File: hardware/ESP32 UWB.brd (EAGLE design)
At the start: 72.3 x 32.6 mm, 55 parts, among them J2 HEADER-12P-2.54, J4 10118194-0001LF, Q3 S8050, Q4 S8050, U1 SILICON_LABS_CP2102N-A01-GQFN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, U2 V_REG_MIC2920, U5 DWM1000, U6 ESP32-C3-MINI-1-N4

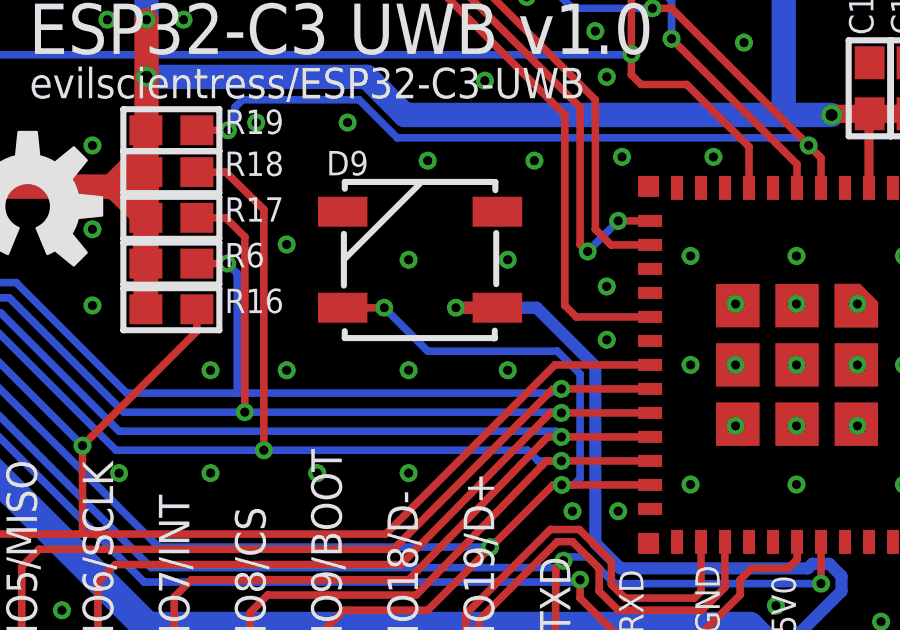
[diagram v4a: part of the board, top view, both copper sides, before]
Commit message: added solder jumper for optionally disabling the ws2812 led
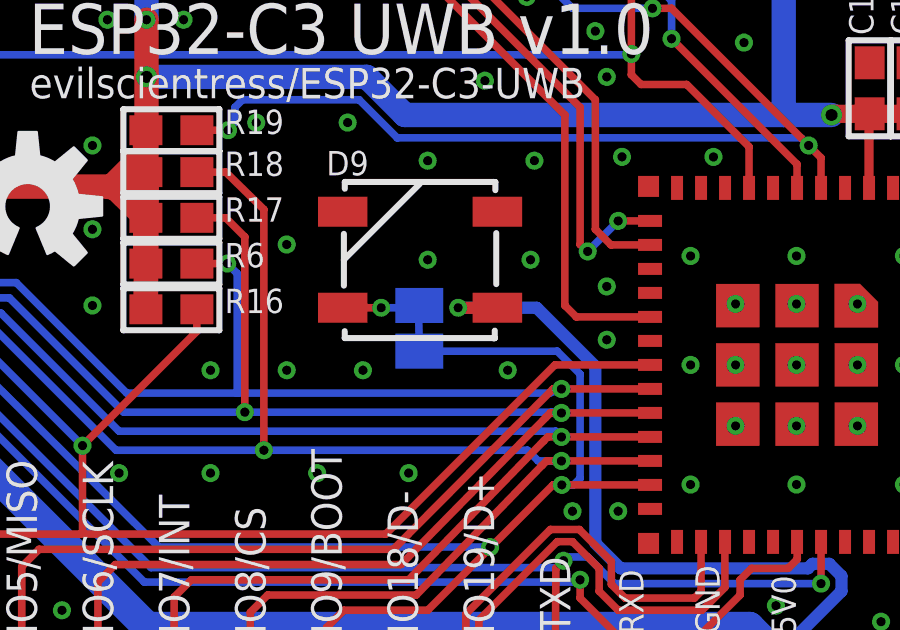
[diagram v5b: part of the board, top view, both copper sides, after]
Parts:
- added SJ1: (no value), jumper:SJ
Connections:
- net IO9: now also SJ1.1, SJ1.2
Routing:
- net IO9: track 96.9 -> 97.8 mm
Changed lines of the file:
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@@
 <setting verticaltext="up"/>
 </settings>
-<grid distance="10" unitdist="mil" unit="mm" style="dots" multiple="1" display="yes" altdistance="1" altunitdist="mil" altunit="mil"/>
+<grid distance="10" unitdist="mil" unit="mil" style="dots" multiple="1" display="yes" altdistance="1" altunitdist="mil" altunit="mil"/>
 <layers>
 <layer number="1" name="Top" color="4" fill="1" visible="yes" active="yes"/>
@@
 <attribute name="VALUE" x="49.594" y="18.11" size="0.6096" layer="27" rot="R180"/>
 </element>
+<element name="SJ1" library="jumper" package="SJ" value="" x="53.8226" y="14.224" smashed="yes" rot="MR90">
+<attribute name="NAME" x="54.9656" y="12.573" size="0.8128" layer="26" font="vector" ratio="18" rot="MR90"/>
+<attribute name="VALUE" x="53.8226" y="14.6241" size="0.02" layer="28" rot="MR90"/>
+</element>
 </elements>
 <signals>
@@
 <via x="56.769" y="12.827" extent="1-16" drill="0.3048"/>
 <via x="53.467" y="9.398" extent="1-16" drill="0.3048"/>
-<via x="53.467" y="12.827" extent="1-16" drill="0.3048"/>
+<via x="51.943" y="12.827" extent="1-16" drill="0.3048"/>
 <via x="43.815" y="9.398" extent="1-16" drill="0.3048"/>
 <via x="42.926" y="17.526" extent="1-16" drill="0.3048"/>
@@
 <contactref element="D9" pad="3"/>
 <via x="58.928" y="8.128" extent="1-16" drill="0.3048"/>
-<via x="56.769" y="16.51" extent="1-16" drill="0.3048"/>
-<via x="53.467" y="16.51" extent="1-16" drill="0.3048"/>
+<via x="57.531" y="16.51" extent="1-16" drill="0.3048"/>
+<via x="54.102" y="16.51" extent="1-16" drill="0.3048"/>
 <contactref element="U1" pad="2"/>
 <contactref element="U1" pad="23"/>
@@
 <contactref element="D6" pad="-"/>
 <contactref element="D9" pad="1"/>
-<wire x1="56.425" y1="14.91" x2="55.042" y2="14.91" width="0.4064" layer="1"/>
-<via x="55.042" y="14.91" extent="1-16" drill="0.3"/>
-<wire x1="55.042" y1="14.91" x2="57.734" y2="14.91" width="0.4064" layer="16"/>
+<wire x1="56.425" y1="14.91" x2="55.1182" y2="14.91" width="0.4064" layer="1"/>
+<via x="55.1182" y="14.91" extent="1-16" drill="0.3"/>
+<wire x1="55.1182" y1="14.91" x2="57.734" y2="14.91" width="0.4064" layer="16"/>
 <wire x1="57.734" y1="14.91" x2="59.69" y2="12.954" width="0.4064" layer="16"/>
 <wire x1="59.69" y1="12.954" x2="59.69" y2="7.0612" width="0.4064" layer="16"/>
@@
 <wire x1="8.9264" y1="29.1068" x2="14.0732" y2="29.1068" width="0.2" layer="1"/>
 <contactref element="D9" pad="4"/>
-<wire x1="51.271" y1="14.91" x2="52.654" y2="14.91" width="0.254" layer="1"/>
-<wire x1="52.654" y1="14.91" x2="54.102" y2="13.462" width="0.254" layer="16"/>
-<wire x1="54.102" y1="13.462" x2="58.42" y2="13.462" width="0.254" layer="16"/>
+<wire x1="51.271" y1="14.91" x2="52.5524" y2="14.91" width="0.254" layer="1"/>
+<wire x1="52.5524" y1="14.91" x2="53.7972" y2="14.91" width="0.254" layer="16"/>
+<wire x1="53.7972" y1="14.91" x2="53.8226" y2="13.462" width="0.254" layer="16"/>
+<wire x1="53.8226" y1="13.462" x2="58.42" y2="13.462" width="0.254" layer="16"/>
 <wire x1="58.42" y1="13.462" x2="59.182" y2="12.7" width="0.254" layer="16"/>
 <wire x1="59.182" y1="12.7" x2="59.182" y2="9.2202" width="0.254" layer="16"/>
 <wire x1="59.182" y1="9.2202" x2="58.9666" y2="9.0048" width="0.254" layer="16"/>
 <wire x1="58.9666" y1="9.0048" x2="58.5724" y2="9.0048" width="0.254" layer="16"/>
-<via x="52.654" y="14.91" extent="1-16" drill="0.3"/>
+<via x="52.5524" y="14.91" extent="1-16" drill="0.3"/>
 <via x="58.5724" y="9.0048" extent="1-16" drill="0.3"/>
 <wire x1="58.2804" y1="9.0048" x2="58.5724" y2="9.0048" width="0.254" layer="1"/>
+<contactref element="SJ1" pad="2"/>
+<contactref element="SJ1" pad="1"/>
+<wire x1="53.7972" y1="14.91" x2="53.8226" y2="14.986" width="0.2" layer="16"/>
 </signal>
 <signal name="IO10">

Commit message: Updated SJ Package to my own (smaller) version
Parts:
- SJ1: device jumper:SJ -> isystems:SJ_S
- moved SJ1 0.10 mm to (53.8, 14.3), turned to 270 degrees
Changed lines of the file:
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@@
 <attribute name="VALUE" x="49.594" y="18.11" size="0.6096" layer="27" rot="R180"/>
 </element>
-<element name="SJ1" library="jumper" package="SJ" value="" x="53.8226" y="14.224" smashed="yes" rot="MR90">
-<attribute name="NAME" x="54.9656" y="12.573" size="0.8128" layer="26" font="vector" ratio="18" rot="MR90"/>
-<attribute name="VALUE" x="53.8226" y="14.6241" size="0.02" layer="28" rot="MR90"/>
+<element name="SJ1" library="isystems" package="SJ_S" value="" x="53.848" y="14.3256" smashed="yes" rot="MR270">
+<attribute name="NAME" x="52.705" y="15.9766" size="0.8128" layer="26" font="vector" ratio="18" rot="MR270"/>
+<attribute name="VALUE" x="53.848" y="13.9255" size="0.02" layer="28" rot="MR270"/>
 </element>
 </elements>
@@
 <via x="15.0114" y="24.3586" extent="1-16" drill="0.3"/>
 <wire x1="8.9264" y1="29.1068" x2="14.0732" y2="29.1068" width="0.2" layer="1"/>
-<contactref element="D9" pad="4"/>
-<wire x1="51.271" y1="14.91" x2="52.5524" y2="14.91" width="0.254" layer="1"/>
-<wire x1="52.5524" y1="14.91" x2="53.7972" y2="14.91" width="0.254" layer="16"/>
-<wire x1="53.7972" y1="14.91" x2="53.8226" y2="13.462" width="0.254" layer="16"/>
-<wire x1="53.8226" y1="13.462" x2="58.42" y2="13.462" width="0.254" layer="16"/>
-<wire x1="58.42" y1="13.462" x2="59.182" y2="12.7" width="0.254" layer="16"/>
+<wire x1="58.1564" y1="13.7256" x2="59.182" y2="12.7" width="0.254" layer="16"/>
 <wire x1="59.182" y1="12.7" x2="59.182" y2="9.2202" width="0.254" layer="16"/>
 <wire x1="59.182" y1="9.2202" x2="58.9666" y2="9.0048" width="0.254" layer="16"/>
 <wire x1="58.9666" y1="9.0048" x2="58.5724" y2="9.0048" width="0.254" layer="16"/>
-<via x="52.5524" y="14.91" extent="1-16" drill="0.3"/>
 <via x="58.5724" y="9.0048" extent="1-16" drill="0.3"/>
 <wire x1="58.2804" y1="9.0048" x2="58.5724" y2="9.0048" width="0.254" layer="1"/>
 <contactref element="SJ1" pad="2"/>
+<wire x1="53.848" y1="13.7256" x2="58.1564" y2="13.7256" width="0.254" layer="16"/>
+<contactref element="D9" pad="4"/>
 <contactref element="SJ1" pad="1"/>
-<wire x1="53.7972" y1="14.91" x2="53.8226" y2="14.986" width="0.2" layer="16"/>
+<wire x1="51.271" y1="14.91" x2="52.5524" y2="14.91" width="0.254" layer="1"/>
+<wire x1="52.5524" y1="14.91" x2="53.7972" y2="14.91" width="0.254" layer="16"/>
+<via x="52.5524" y="14.91" extent="1-16" drill="0.3"/>
+<wire x1="53.7972" y1="14.91" x2="53.848" y2="14.91" width="0.4064" layer="16"/>
+<wire x1="53.848" y1="14.91" x2="53.848" y2="14.9256" width="0.254" layer="16"/>
+<wire x1="53.848" y1="14.9256" x2="53.848" y2="13.7256" width="0.254" layer="16"/>
 </signal>
 <signal name="IO10">

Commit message: renumbered parts
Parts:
- removed C14: 10u, isystems:0603
- removed C15: 100n, isystems:0603
- removed D9: WS2812B, SparkFun-LED:WS2812B
- removed R23: 470R, isystems:0603
- removed U6: ESP32-C3-MINI-1-N4, ESP32-C3-MINI-1-N4:XCVR_ESP32-C3-MINI-1-N4
- added C1: 10u, isystems:0603
- added C2: 100n, isystems:0603
- added LED1: BLUE, isystems:CHIPLED_0603_NOOUTLINE
- added R5: 1K, isystems:0603
- added U3: SILICON_LABS_CP2102N-A01-GQFN28SILICON_LABS_CP2102N-A01-GQF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, Silicon Labs - CP2102N-A01-GQFN28:SILICON_LABS_CP2102N-A01-GQFN28_3
- C10: value 100n -> 10u
- C11: value 4.7uF -> 100n
- C12: value 100nf -> 4.7uF; device microbuilder:0603-NO -> isystems:0603
- C5: value 10u -> 100n
- C7: value 100n -> 100nf; device isystems:0603 -> microbuilder:0603-NO
- D1: value GREEN -> B5819WS; device microbuilder:CHIPLED_0805_NOOUTLINE -> Discrete:SOD323
- D3: value GREEN -> WS2812B; device microbuilder:CHIPLED_0805_NOOUTLINE -> SparkFun-LED:WS2812B
- D6: value B5819WS -> GREEN; device Discrete:SOD323 -> microbuilder:CHIPLED_0805_NOOUTLINE
- D7: value BLUE -> GREEN; device isystems:CHIPLED_0603_NOOUTLINE -> microbuilder:CHIPLED_0805_NOOUTLINE
- R10: value 470R -> 10k
- R11, R8: value 1K -> NC
- R12, R13: value 1K -> 470R
- R15: value 10K -> 1K
- R16: value 10k -> 1k
- R17: value 10k -> 1K
- R18: value NC -> 10K
- R19: value NC -> 470R
- R3: value 470R -> 10K
- R4: value 1k -> 10K
- R6: value NC -> 1K
- R7: value 10K -> NC
- R9: value 10K -> 10k
- U1: value SILICON_LABS_CP2102N-A01-GQFN28SILICON_LABS_CP2102N-A01-GQFN28_0_3 -> AMS1117-3.3; device Silicon Labs - CP2102N-A01-GQFN28:SILICON_LABS_CP2102N-A01-GQFN28_3 -> SparkFun-PowerIC:SOT223
- U2: value V_REG_MIC2920 -> ESP32-C3-MINI-1-N4; device SparkFun-PowerIC:SOT223 -> ESP32-C3-MINI-1-N4:XCVR_ESP32-C3-MINI-1-N4
- moved C6 62.5 mm to (68.8, 22.2), turned to 90 degrees
- moved C8 59.9 mm to (70.2, 22.2), turned to 90 degrees
- moved U2 58.4 mm to (69.1, 13.0), turned to 270 degrees
- moved D3 45.9 mm to (53.8, 16.5), turned to 180 degrees
- moved R10 42.0 mm to (45.6, 14.9)
- moved R9 40.2 mm to (45.6, 17.9), turned to 0 degrees
- moved R7 40.0 mm to (45.6, 20.8), turned to 0 degrees
- moved R6 35.5 mm to (12.4, 29.1), turned to 90 degrees
- moved R11 34.4 mm to (45.6, 16.4), turned to 0 degrees
- moved D2 33.5 mm to (10.5, 1.39), turned to 90 degrees
- moved R16 31.6 mm to (14.1, 11.7), turned to 270 degrees
- moved D1 31.2 mm to (6.42, 6.97)
- moved R18 29.7 mm to (16.6, 12.5), turned to 270 degrees
- moved C11 29.4 mm to (35.4, 19.8), turned to 90 degrees
- moved C4 29.3 mm to (14.1, 1.40), turned to 0 degrees
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- renumbered D8 to LED2, FLASH to SW2, J4 to J3, Q3 to Q1, Q4 to Q2, RST to SW1, U5 to U4
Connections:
- net +3V3: now also C12.1, C5.1, D2.A, R10.1, R11.1, R12.1, R13.1, R16.2, R3.2, R7.1, R8.1, R9.1, U1.3, U3.6, U3.7; no longer C14.1, C15.1, D3.A, R1.1, R16.1, R17.1, R18.1, R19.1, R2.1, R6.1, R7.2, R9.2, U1.6, U1.7, U6.3
- net D+: now also U3.4; no longer U1.4
- net D-: now also U3.5; no longer U1.5
- net DTR: now also R6.2, U3.28; no longer R12.2, U1.28
- net GND: now also C1.2, C2.2, D3.3, D6.C, D7.C, R18.2, R2.1, U2.1, U2.11, U2.14, U2.36, U2.37, U2.38, U2.39, U2.40, U2.41, U2.42, U2.43, U2.44, U2.45, U2.46, U2.47, U2.48, U2.49_1, U2.49_2, U2.49_3, U2.49_4, U2.49_5, U2.49_6, U2.49_7, U2.49_8, U2.49_9, U2.50, U2.51, U2.52, U2.53, U3.2, U3.23, U3.27, U3.29, U3.3; no longer C14.2, C15.2, D1.C, D2.C, D9.3, R15.2, R3.1, U1.23, U1.27, U1.29, U1.3, U6.1, U6.11, U6.14, U6.2, U6.36, U6.37, U6.38, U6.39, U6.40, U6.41, U6.42, U6.43, U6.44, U6.45, U6.46, U6.47, U6.48, U6.49_1, U6.49_2, U6.49_3, U6.49_4, U6.49_5, U6.49_6, U6.49_7, U6.49_8, U6.49_9, U6.50, U6.51, U6.52, U6.53
- net IO0: now also R15.1, U2.12; no longer R13.1, U6.12
- net IO1: now also R17.1, U2.13; no longer R8.1, U6.13
- net IO10: now also U2.16; no longer U6.16
- net IO18: now also U2.26; no longer U6.26
- net IO19: now also U2.27; no longer U6.27
- net IO2: now also R7.2, U2.5; no longer R19.2, U6.5
- net IO3: now also U2.6; no longer U6.6
- net IO4/MOSI: now also R10.2, U2.18; no longer R16.2, U6.18
- net IO5/MISO: now also R11.2, U2.19; no longer R6.2, U6.19
- net IO6/SCLK: now also R9.2, U2.20; no longer R17.2, U6.20
- net IO7: now also R18.1, U2.21; no longer R15.1, U6.21
- net IO8/CS: now also R8.2, U2.22; no longer R18.2, U6.22
- net IO9: now also D3.4, R1.2, R4.1, U2.23; no longer D9.4, R10.2, R7.1, U6.23
- net LEDRX: now also R20.1; no longer R21.1
- net LEDRXOK: now also R22.1; no longer R23.1
- net LEDSFD: now also R21.1; no longer R22.1
- net LEDTX: now also R19.1; no longer R20.1
- net N$1: now also D4.A, R19.2; no longer D1.A, R20.2
- net N$10: now also R17.2; no longer R8.2
- net N$11: now also R15.2; no longer R13.2
- net N$13: now also R6.1; no longer R12.1
- net N$14: now also R5.1; no longer R11.1
- net N$15: now also R1.1; no longer R10.1
- net N$16: now also D5.A, R20.2; no longer D2.A, R21.2
- net N$17: now also D6.A, R21.2; no longer D4.A, R22.2
- net N$18: now also D7.A, R22.2; no longer D5.A, R23.2
- net N$2: now also LED1.A, R12.2; no longer D7.A, R1.2
- net N$3: now also LED1.C, U3.19; no longer D7.C, U1.19
- net N$4: now also R13.2; no longer R2.2
- net N$5: now also D2.C, R2.2; no longer D3.C, R3.2
- net N$6: now also U3.18; no longer U1.18
- net N$8: now also R16.1, U3.9; no longer R4.1, U1.9
- net RESET: now also C7.1, R3.1, U2.8; no longer C12.1, R9.1, U6.8
- net RTS: now also R5.2, U3.24; no longer R11.2, U1.24
- net RXD: now also U2.30, U3.26; no longer U1.26, U6.30
- net TXD: now also U2.31, U3.25; no longer U1.25, U6.31
- net VBUS: now also C1.1, C2.1, D1.+, U3.8; no longer C5.1, C7.1, D6.+, U1.8
- net VDD5V: now also D1.-, D3.1, U1.1; no longer D6.-, D9.1, U2.1

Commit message: replaced footprint of C7
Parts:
- C7: value 100nf -> 100n; device microbuilder:0603-NO -> isystems:0603
- moved C7 0.09 mm to (6.27, 24.7)
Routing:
- net RESET: track 96.7 -> 93.5 mm
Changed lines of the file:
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@@
 <attribute name="VALUE" x="4.464" y="26.9046" size="0.4064" layer="27" font="vector" ratio="10" rot="R180"/>
-</element>
-<element name="C7" library="microbuilder" package="0603-NO" value="100nf" x="6.242" y="24.6594" smashed="yes" rot="R180">
-<attribute name="NAME" x="7.7153" y="23.8517" size="0.8128" layer="25" font="vector" ratio="18" rot="R180"/>
-<attribute name="VALUE" x="4.464" y="25.4214" size="0.4064" layer="27" font="vector" ratio="10" rot="R180"/>
 </element>
 <element name="R1" library="isystems" package="0603" value="470R" x="6.242" y="29.4936" smashed="yes">
@@
 <attribute name="VALUE" x="53.848" y="13.9255" size="0.02" layer="28" rot="MR270"/>
 </element>
+<element name="C7" library="isystems" package="0603" value="100n" x="6.2738" y="24.7396" rot="R180"/>
 </elements>
 <signals>
 <signal name="GND">
-<contactref element="C7" pad="2"/>
 <contactref element="SW1" pad="1"/>
 <contactref element="SW2" pad="1"/>
@@
 <wire x1="12.43" y1="18.786" x2="12.43" y2="17.399" width="0.2" layer="1"/>
 <wire x1="12.43" y1="17.399" x2="12.319" y2="17.399" width="0.2" layer="1"/>
+<contactref element="C7" pad="2"/>
 </signal>
 <signal name="+3V3">
@@
 <contactref element="Q2" pad="3"/>
 <contactref element="R3" pad="1"/>
-<contactref element="C7" pad="1"/>
 <contactref element="SW1" pad="2"/>
 <contactref element="J1" pad="3"/>
 <wire x1="7.0124" y1="26.164" x2="7.092" y2="26.1426" width="0.254" layer="1"/>
-<wire x1="7.092" y1="21.57" x2="7.092" y2="24.6594" width="0.254" layer="1"/>
 <via x="14.4272" y="27.813" extent="1-16" drill="0.3048"/>
 <wire x1="19.6596" y1="27.813" x2="24.13" y2="23.3426" width="0.254" layer="16"/>
@@
 <wire x1="60.8646" y1="23.3426" x2="60.89" y2="23.368" width="0.254" layer="16"/>
 <via x="60.89" y="23.368" extent="1-16" drill="0.3048"/>
-<wire x1="7.092" y1="24.6594" x2="7.6414" y2="24.6594" width="0.254" layer="1"/>
-<wire x1="7.6414" y1="24.6594" x2="8.001" y2="25.019" width="0.254" layer="1"/>
 <wire x1="7.092" y1="26.1426" x2="7.6394" y2="26.1426" width="0.254" layer="1"/>
 <wire x1="7.6394" y1="26.1426" x2="8.0244" y2="25.7576" width="0.254" layer="1"/>
 <wire x1="8.0244" y1="25.7576" x2="8.9108" y2="25.7576" width="0.254" layer="1"/>
 <wire x1="8.0244" y1="25.7576" x2="8.001" y2="25.7342" width="0.254" layer="1"/>
-<wire x1="8.001" y1="25.7342" x2="8.001" y2="25.019" width="0.254" layer="1"/>
+<wire x1="8.001" y1="25.7342" x2="8.001" y2="25.0952" width="0.254" layer="1"/>
 <wire x1="8.9108" y1="25.7576" x2="8.9108" y2="23.9568" width="0.2" layer="1"/>
 <wire x1="8.9108" y1="23.9568" x2="9.398" y2="23.4696" width="0.2" layer="1"/>
@@
 <wire x1="2.413" y1="11.176" x2="2.413" y2="10.1572" width="0.254" layer="1"/>
 <wire x1="2.413" y1="10.1572" x2="2.4166" y2="10.1536" width="0.254" layer="1"/>
+<contactref element="C7" pad="1"/>
+<wire x1="7.1238" y1="24.7396" x2="7.6454" y2="24.7396" width="0.254" layer="1"/>
+<wire x1="7.6454" y1="24.7396" x2="8.001" y2="25.0952" width="0.254" layer="1"/>
+<wire x1="7.092" y1="21.57" x2="9.398" y2="23.4696" width="0" layer="19" extent="1-1"/>
 </signal>
 <signal name="RXD">
